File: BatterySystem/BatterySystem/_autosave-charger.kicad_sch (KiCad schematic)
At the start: 22 parts, among them U2 BQ25895RTW

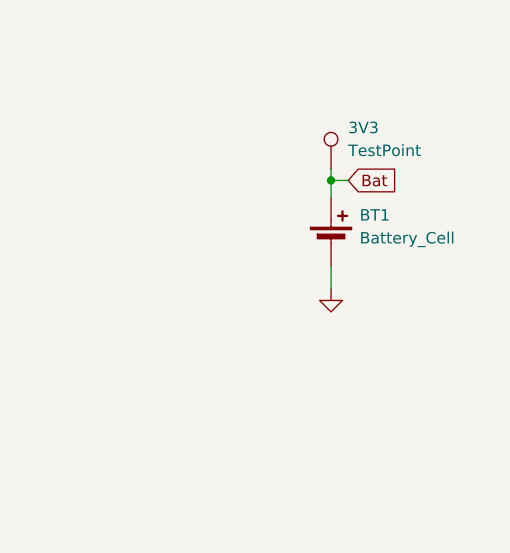
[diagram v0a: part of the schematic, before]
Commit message: Buck converter gedaan en meer test point toegevoegd
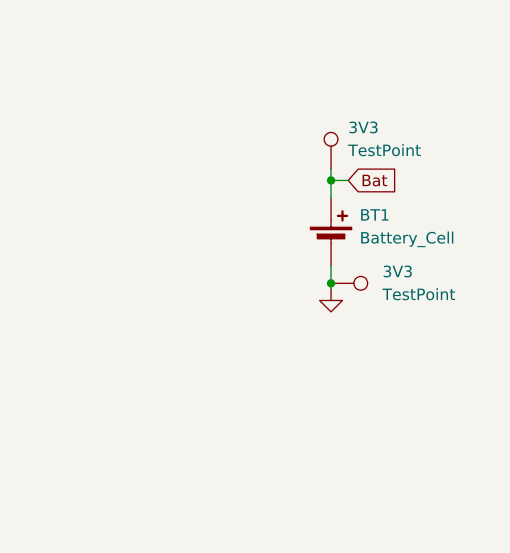
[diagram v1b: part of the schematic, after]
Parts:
- added 3V3: TestPoint, TestPoint:TestPoint_Keystone_5005-5009_Compact, symbol Connector:TestPoint
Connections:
- net GND: now also 3V3.1
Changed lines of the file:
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@@
   (junction (at 152.4 88.9) (diameter 0) (color 0 0 0 0)
+  )
+  (junction (at 230.505 97.79) (diameter 0) (color 0 0 0 0)
   )
   (junction (at 147.32 81.28) (diameter 0) (color 0 0 0 0)
@@
     (stroke (width 0) (type default))
   )
+  (wire (pts (xy 230.505 97.79) (xy 230.505 98.425))
+    (stroke (width 0) (type default))
+  )
   (wire (pts (xy 101.6 74.93) (xy 101.6 76.2))
     (stroke (width 0) (type default))
   )
-  (wire (pts (xy 230.505 95.885) (xy 230.505 98.425))
+  (wire (pts (xy 230.505 95.885) (xy 230.505 97.79))
     (stroke (width 0) (type default))
   )
@@
         (path "/087df5f5-f8bd-4aad-837d-9ee553cf1b81/c2cf6bc5-c7a7-4536-bd5f-b8479578647d"
           (reference "C7") (unit 1)
+        )
+      )
+    )
+  )
+  (symbol (lib_id "Connector:TestPoint") (at 230.505 97.79 270) (unit 1)
+    (in_bom yes) (on_board yes) (dnp no) (fields_autoplaced)
+    (property "Reference" "3V3" (at 236.22 96.52 90)
+      (effects (font (size 1.27 1.27)) (justify left))
+    )
+    (property "Value" "TestPoint" (at 236.22 99.06 90)
+      (effects (font (size 1.27 1.27)) (justify left))
+    )
+    (property "Footprint" "TestPoint:TestPoint_Keystone_5005-5009_Compact" (at 230.505 102.87 0)
+      (effects (font (size 1.27 1.27)) hide)
+    )
+    (property "Datasheet" "~" (at 230.505 102.87 0)
+      (effects (font (size 1.27 1.27)) hide)
+    )
+    (pin "1")
+    (instances
+      (project "BatterySystem"
+        (path "/087df5f5-f8bd-4aad-837d-9ee553cf1b81/a03965c6-cfc0-427e-8817-8deee22f0563"
+          (reference "3V3") (unit 1)
+        )
+        (path "/087df5f5-f8bd-4aad-837d-9ee553cf1b81/c2cf6bc5-c7a7-4536-bd5f-b8479578647d"
+          (reference "GND2") (unit 1)
         )
       )
@@
         )
         (path "/087df5f5-f8bd-4aad-837d-9ee553cf1b81/c2cf6bc5-c7a7-4536-bd5f-b8479578647d"
-          (reference "Bat_test_point") (unit 1)
-        )
-      )
+          (reference "Bat_test_point1") (unit 1)
+        )
+      )
